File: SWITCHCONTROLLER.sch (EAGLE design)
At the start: 124 parts, among them IC1 MCP23017SO, IC2 MCP23017SO, IC3 MCP23017SO, IC4 MCP23017SO, IC5 MCP23017SO, IC6 MCP23017SO, J1 RJ45-X8, J2 RJ45-X8, J3 RJ45-X8, J5 M06-PIN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

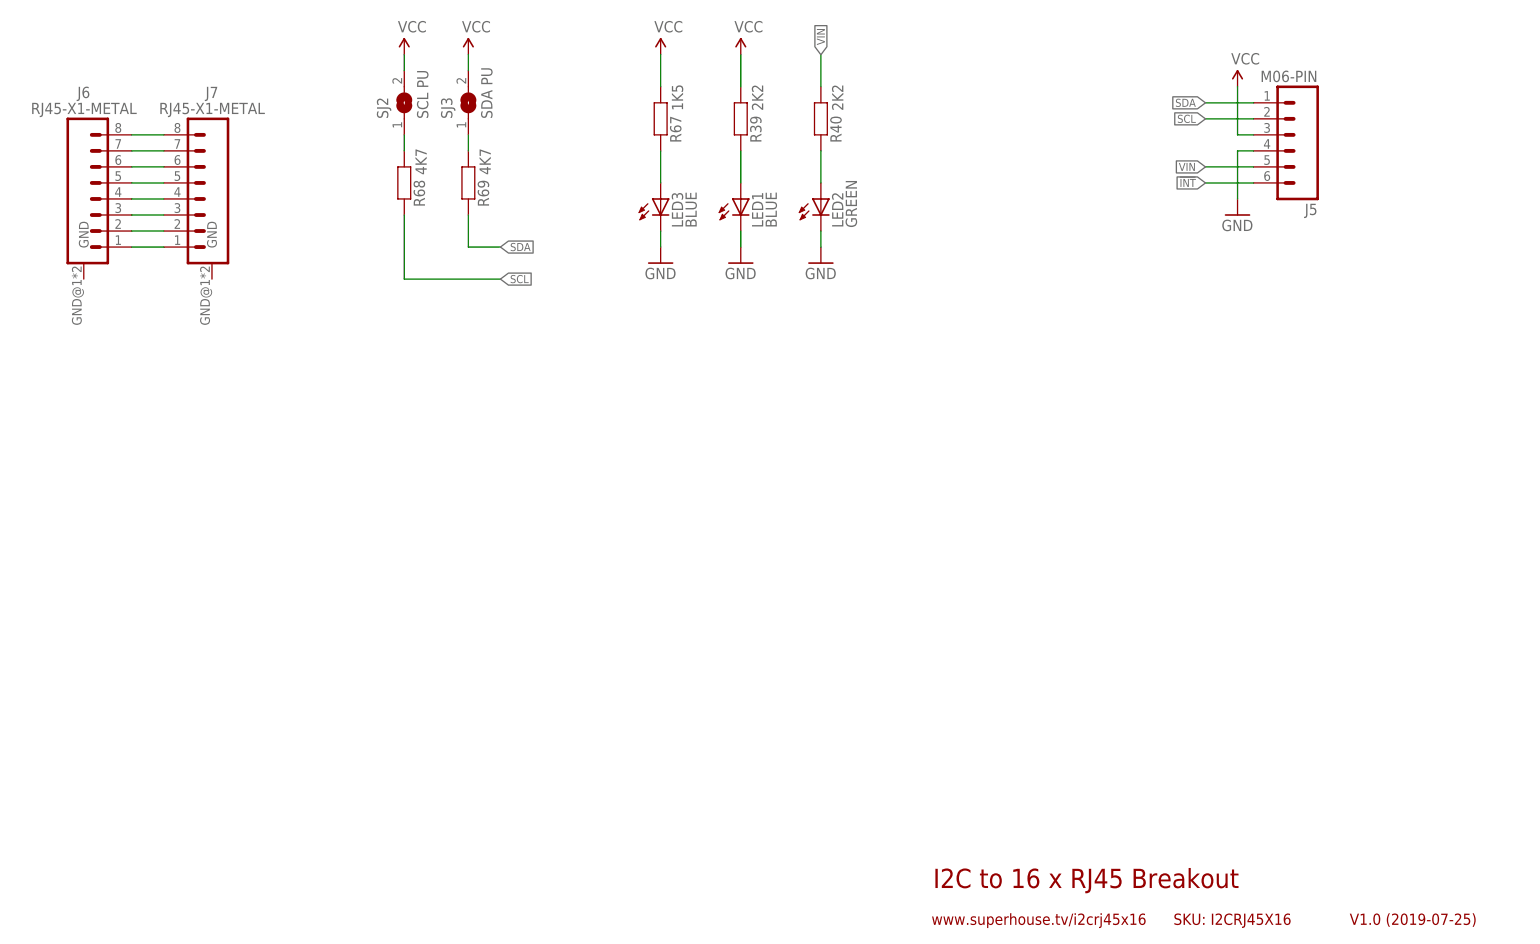
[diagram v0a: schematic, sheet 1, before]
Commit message: Added DC power jack and screw terminal
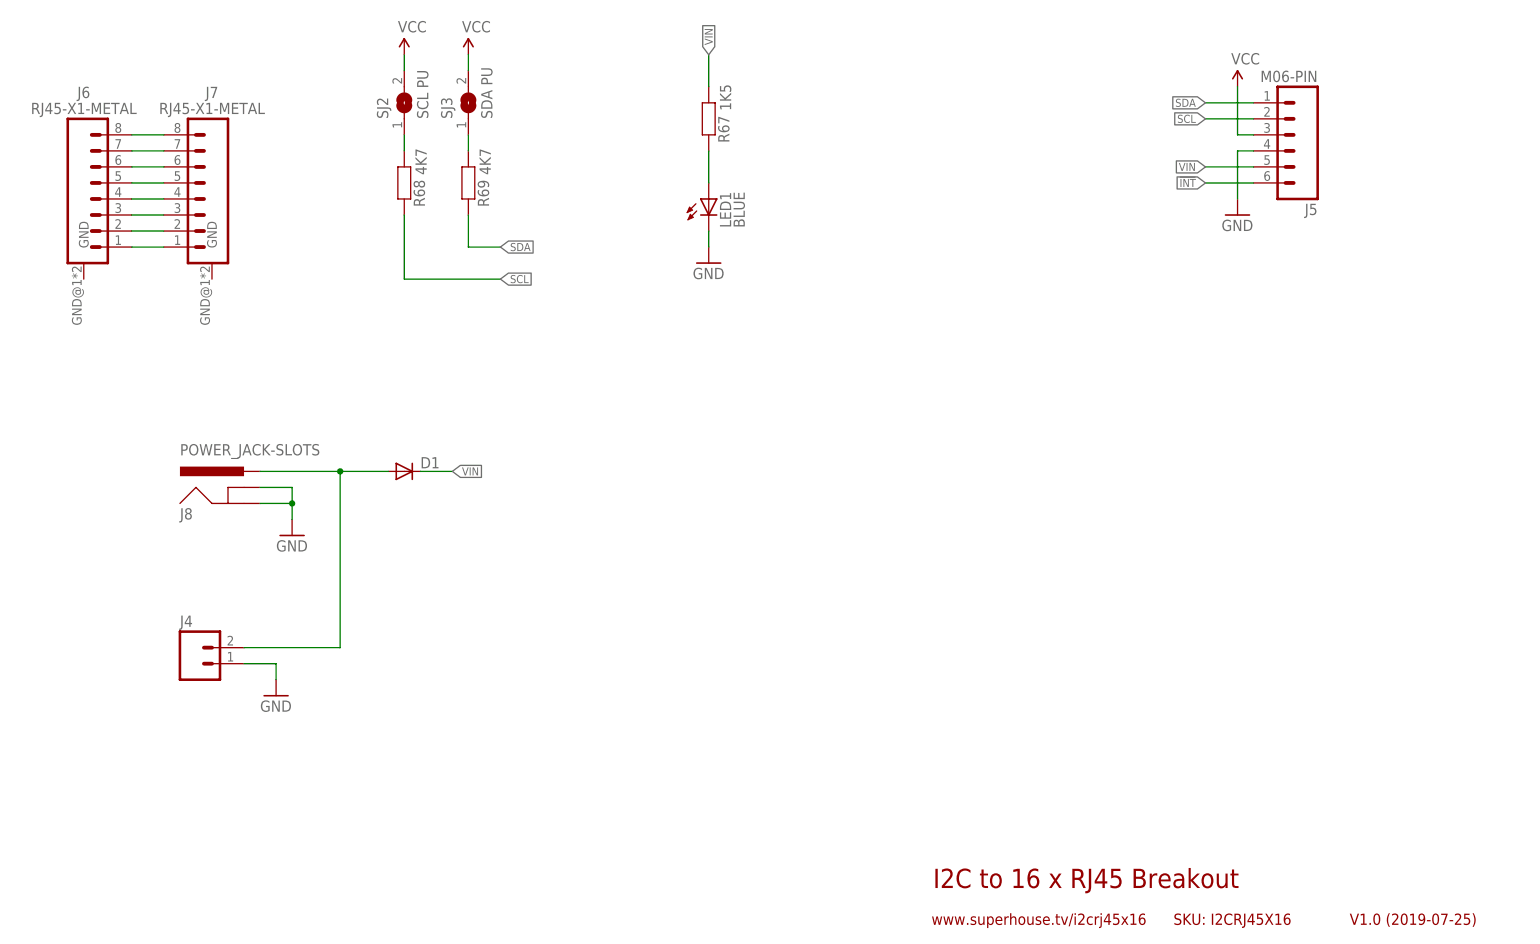
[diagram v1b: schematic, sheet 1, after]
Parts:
- removed LED2: GREEN, SuperHouse-LEDs:LED0603
- removed LED3: BLUE, SuperHouse-LEDs:LED3MM
- removed R39, R40: 2K2, SuperHouse-DiscreteSemi:RESISTOR0603
- added D1: (no value), SuperHouse-DiscreteSemi:DIODESMA
- added J4: (no value), SuperHouse-Connectors:M02-SCREW-3.5MM
- added J8: POWER_JACK-SLOTS, SuperHouse-Connectors:POWER_JACK-SLOTS
- LED1: device SuperHouse-LEDs:LED0603 -> SuperHouse-LEDs:LED3MM
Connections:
- removed net N$7: LED1.A, R39.1
- removed net N$8: LED2.A, R40.1
- new net N$18: D1.A, J4.2, J8.PWR
- net GND: now also J4.1, J8.GND, J8.GNDBREAK; no longer LED2.C, LED3.C
- net N$13: now also LED1.A; no longer LED3.A
- net VCC: no longer R39.2, R67.2
- net VIN: now also D1.C, R67.2; no longer R40.2
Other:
- moved on the sheet: LED1, R67
